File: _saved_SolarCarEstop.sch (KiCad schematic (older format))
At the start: 49 parts

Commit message: Add buck converter and 555 charge pump
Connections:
- net GND: now also J?.1 (Pin_1)
- net MOS_DRAIN: now also D?.1 (K), J?.1 (Pin_1); no longer J?.1 (Pin_1)
- net MOS_SOURCE: now also J?.1 (Pin_1)
- removed net vBatt: D?.1 (K), J?.1 (Pin_1), J?.1 (Pin_1)
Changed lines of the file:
@@
 	1    0    0    -1
 $EndComp
-Text Label 10250 1800 2    50   ~ 0
-MOS_DRAIN
-Text Label 10250 1450 2    50   ~ 0
-vBatt
 $Comp
 L power:GND #PWR?
@@
 	1    0    0    -1
 $EndComp
+Wire Wire Line
+	10250 750  9900 750
+Text Label 9900 750  2    50   ~ 0
+MOS_DRAIN
+$Comp
+L power:GND #PWR?
+U 1 1 5F792EB8
+P 10250 1800
+F 0 "#PWR?" H 10250 1550 50  0001 C CNN
+F 1 "GND" H 10255 1627 50  0000 C CNN
+F 2 "" H 10250 1800 50  0001 C CNN
+F 3 "" H 10250 1800 50  0001 C CNN
+	1    10250 1800
+	1    0    0    -1
+$EndComp
+Text Label 10250 1450 2    50   ~ 0
+MOS_SOURCE
 $EndSCHEMATC

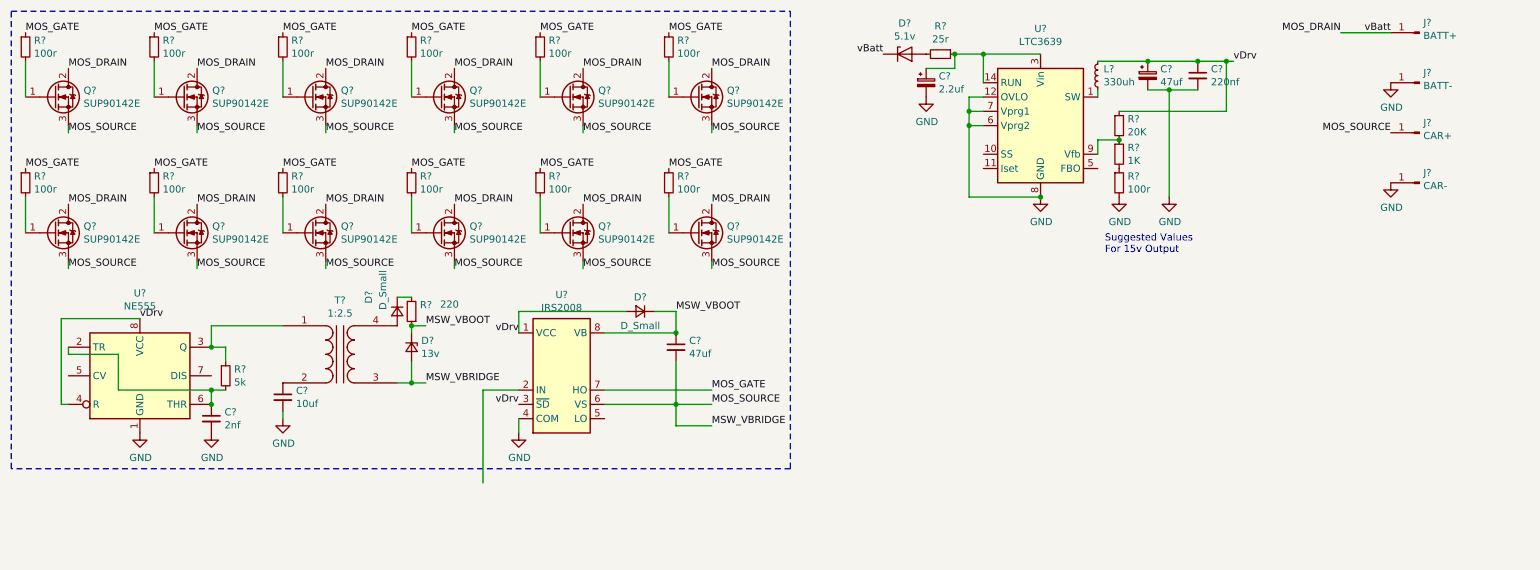
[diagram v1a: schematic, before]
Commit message: Add emergency button, BMS fault output, and BMS fault input
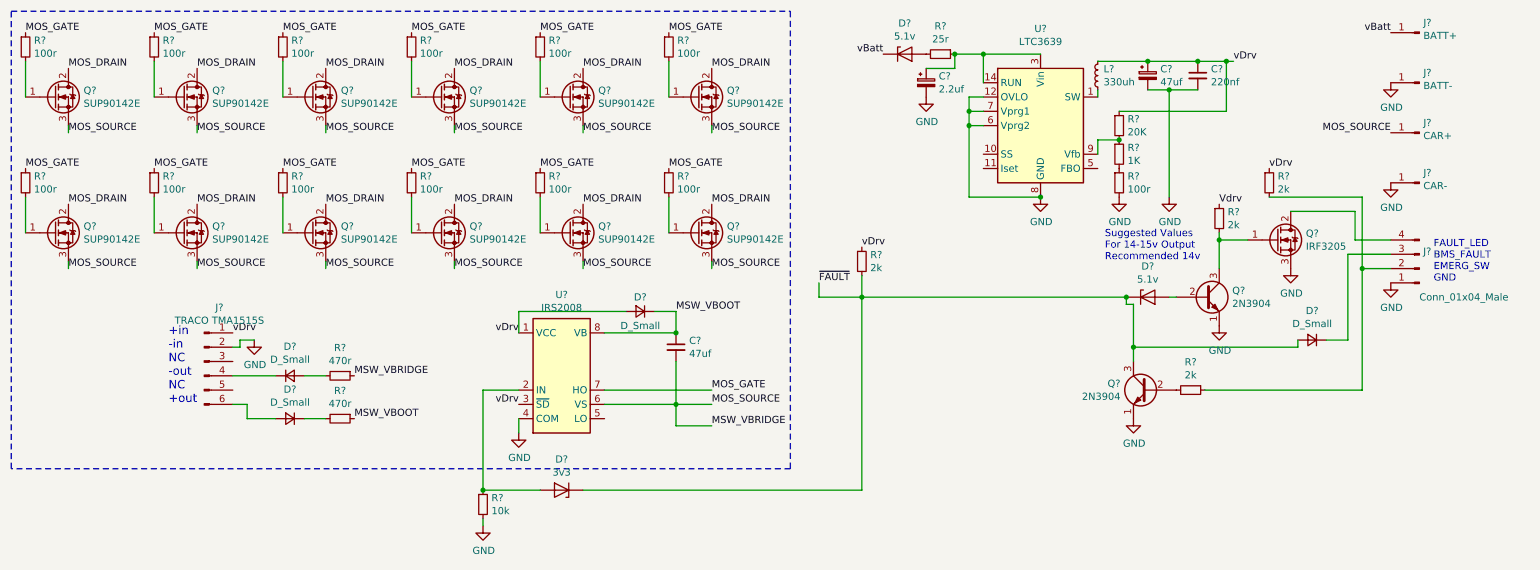
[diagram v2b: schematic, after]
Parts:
- removed C?: 10uf, symbol Device:C_Small
- removed C?: 2nf, symbol Device:C_Small
- removed D?: D_Small, symbol Device:D_Small
- removed D?: 13v, symbol Device:D_Zener_Small
- removed R?: 220, symbol Device:R_Small
- removed R?: 5k, symbol Device:R_Small
- removed T?: 1:2.5, symbol Device:Transformer_1P_1S
- removed U?: NE555, symbol Timer:NE555
- added D? (x3): D_Small, symbol Device:D_Small
- added D?: 5.1v, symbol Device:D_Zener
- added D?: 3v3, symbol Device:D_Zener
- added J?: TRACO TMA1515S, symbol Connector:Conn_01x06_Male
- added J?: Conn_01x04_Male, symbol Connector:Conn_01x04_Male
- added Q?: IRF3205, Package_TO_SOT_THT:TO-220-3_Vertical, symbol Transistor_FET:IRF3205
- added Q? (x2): 2N3904, Package_TO_SOT_THT:TO-92_Inline, symbol Transistor_BJT:2N3904
- added R? (x2): 470r, symbol Device:R_Small
- added R? (x4): 2k, symbol Device:R_Small
- added R?: 10k, symbol Device:R_Small
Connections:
- net GND: now also J?.1 (Pin_1), J?.2 (Pin_2), Q?.1 (E), Q?.1 (E), Q?.3 (S), R?.2
- net MOS_DRAIN: no longer D?.1 (K), J?.1 (Pin_1)
- net MOS_SOURCE: now also R?.1
- net MSW_VBOOT: now also R?.1
- net vDrv: now also J?.1 (Pin_1), R?.1, R?.1
- net at U?.2 (IN): now also D?.2 (A), R?.1
- new net: D?.1 (K), J?.4 (Pin_4)
- new net: D?.2 (A), J?.6 (Pin_6)
- new net: D?.2 (A), R?.2
- new net: D?.1 (K), R?.2
- new net: J?.2 (Pin_2), R?.1, R?.2
- new net: D?.1 (K), J?.3 (Pin_3)
- new net: J?.4 (Pin_4), Q?.2 (D)
- new net: Q?.1 (G), Q?.3 (C), R?.2
- new net: D?.2 (A), Q?.2 (B)
- new net: Q?.2 (B), R?.2
- new net Vdrv: R?.1
- new net vBatt: D?.1 (K), J?.1 (Pin_1)
- new net ~FAULT: D?.1 (K), D?.1 (K), D?.2 (A), Q?.3 (C), R?.2
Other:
- note added: "+in\n-in\nNC\n-out\nNC\n+out"
- note added: "FAULT_LED\nBMS_FAULT\nEMERG_SW\nGND"
- note added: "Suggested Values\nFor 14-15v Output\nRecommended 14v"
- note removed: "Suggested Values\nFor 15v Output"
